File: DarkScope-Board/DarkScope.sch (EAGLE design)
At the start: 5 parts, among them IC1 ATSAME70Q21A-AN, X1 1-227161-0, X2 1-227161-0, X3 1-227161-0, X4 1-227161-0

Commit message: Added Circuits
Added circuitry for 4 channels and Op amps
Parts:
- removed X4: 1-227161-0, con-coax:1-227161-0
- added C1, C10, C18, C19, C27, C28, C36, C9: 0.1uf, rcl:C-EUC0603
- added C11, C2, C20, C29: 220pf, rcl:C-EUC0603
- added C12, C21, C3, C30: 3pf, rcl:C-EUC0603
- added C13, C22, C31, C4: 1PF, rcl:C-EUC0603
- added C14, C15, C23, C24, C32, C33, C5, C6: 30pf, rcl:C-TRIMM3018_11
- added C16, C17, C25, C26, C34, C35, C7, C8: 120pf, rcl:C-EUC0603
- added D1, D2, D3, D4: ss14, diode:SCHOTTKY-DIODESMD
- added IC2, IC3, IC4, IC5: TL084D, linear:TL084D
- added K1, K2, K3, K4: 4-1462037-0 (3V Version), SamacSys_Parts:4-1462037-0
- added R1, R19, R37, R55: 10M, rcl:R-US_R0603
- added R10, R14, R15, R28, R32, R33, R46, R50, R51, R64, R68, R69: 120, rcl:R-US_R0603
- added R11, R18, R29, R36, R47, R54, R65, R72: 1k, rcl:R-US_R0603
- added R12, R30, R48, R66: 3k, rcl:R-US_R0603
- added R13, R31, R49, R67: 1.5k, rcl:R-US_R0603
- added R16, R17, R21, R3, R34, R35, R39, R52, R53, R57, R70, R71: 100k, rcl:R-US_R0603
- added R2, R20, R38, R56: 1M, rcl:R-US_R0603
- added R22, R4, R40, R58: 1.8M, rcl:R-US_R0603
- added R23, R41, R5, R59: 2M, rcl:R-US_R0603
- added R24, R42, R6, R60: 200k, rcl:R-US_R0603
- added R25, R43, R61, R7: 20k, rcl:R-US_R0603
- added R26, R44, R62, R8: 300, rcl:R-US_R0603
- added R27, R45, R63, R9: 180, rcl:R-US_R0603
- added T1, T10, T11, T12, T13, T14, T15, T16, T17, T18, T19, T2, T20, T21, T22, T23, T24, T25, T26, T27, T28, T29, T3, T30, T31, T32, T33, T34, T35, T36, T37, T38, T39, T4, T40, T5, T6, T7, T8, T9: (no value), DC_LOAD_AU:BC817-40-NPN-SOT23-BEC
- added X5: 1-227161-0, con-coax:1-227161-0
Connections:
- new net +5V: R12.2, R30.2, R48.2, R66.2
- new net +5V/2: D1.C, D2.C, D3.C, D4.C, K1.8, K2.8, K3.8, K4.8
- new net GND: C14.A, C15.A, C16.2, C17.2, C18.2, C23.A, C24.A, C25.2, C26.2, C27.2, C32.A, C33.A, C34.2, C35.2, C36.2, C5.A, C6.A, C7.2, C8.2, C9.2, R10.2, R13.1, R2.1, R20.1, R24.2, R25.2, R28.2, R31.1, R38.1, R42.2, R43.2, R46.2, R49.1, R56.1, R6.2, R60.2, R61.2, R64.2, R67.1, R7.2, T1.E, T11.E, T14.C, T21.E, T24.C, T31.E, T34.C, T4.C, X1.2, X2.2, X3.2, X5.2
- new net N$1: D1.A, K1.1, T1.C
- new net N$10: C2.2, R3.1, T5.C
- new net N$100: R62.2, R63.1, T38.C
- new net N$101: R63.2, R64.1, T39.C
- new net N$102: T35.B
- new net N$103: T36.B
- new net N$104: T37.B
- new net N$105: T34.B
- new net N$106: T33.B
- new net N$107: T32.B
- new net N$108: IC5C.+IN, T38.E, T39.E, T40.E
- new net N$109: IC5C.-IN, R65.1, R66.1, R67.2
- new net N$11: C3.2, C5.E, R4.1, R6.1, T6.C
- new net N$110: IC5C.OUT, R65.2, R68.1, R69.2
- new net N$111: C35.1, R68.2
- new net N$112: IC5D.+IN, R69.1, R70.2
- new net N$113: IC5D.OUT, R70.1, R72.2
- new net N$114: C36.1, IC5D.-IN, R71.2
- new net N$115: R71.1
- new net N$116: R72.1
- new net N$12: R10.1, R9.2, T9.C
- new net N$13: IC2B.+IN, T5.E, T6.E, T7.E
- new net N$14: IC2B.-IN, IC2B.OUT, R8.1, T10.C
- new net N$15: T5.B
- new net N$16: T6.B
- new net N$17: T7.B
- new net N$18: T4.B
- new net N$19: T3.B
- new net N$2: T1.B
- new net N$20: T2.B
- new net N$21: IC2C.+IN, T10.E, T8.E, T9.E
- new net N$22: IC2C.-IN, R11.1, R12.1, R13.2
- new net N$23: IC2C.OUT, R11.2, R14.1, R15.2
- new net N$24: C8.1, R14.2
- new net N$25: IC2D.+IN, R15.1, R16.2
- new net N$26: IC2D.OUT, R16.1, R18.2
- new net N$27: C9.1, IC2D.-IN, R17.2
- new net N$28: R17.1
- new net N$29: R18.1
- new net N$3: C1.2, T3.C
- new net N$30: D2.A, K2.1, T11.C
- new net N$31: K2.6, X5.1
- new net N$32: C10.1, K2.7, R19.1, R20.2, T12.C
- new net N$33: K2.5, R19.2
- new net N$34: T11.B
- new net N$35: C10.2, T13.C
- new net N$36: C11.1, C12.1, C13.1, R21.2, R22.2, R23.2, T12.E, T13.E, T14.E
- new net N$37: C11.2, R21.1, T15.C
- new net N$38: C12.2, C14.E, R22.1, R24.1, T16.C
- new net N$39: C13.2, C15.E, C16.1, R23.1, R25.1, T17.C
- new net N$4: K1.6, X1.1
- new net N$40: IC3B.+IN, T15.E, T16.E, T17.E
- new net N$41: IC3B.-IN, IC3B.OUT, R26.1, T20.C
- new net N$42: R26.2, R27.1, T18.C
- new net N$43: R27.2, R28.1, T19.C
- new net N$44: T15.B
- new net N$45: T16.B
- new net N$46: T17.B
- new net N$47: T14.B
- new net N$48: T13.B
- new net N$49: T12.B
- new net N$5: R8.2, R9.1, T8.C
- new net N$50: IC3C.+IN, T18.E, T19.E, T20.E
- new net N$51: IC3C.-IN, R29.1, R30.1, R31.2
- new net N$52: IC3C.OUT, R29.2, R32.1, R33.2
- new net N$53: C17.1, R32.2
- new net N$54: IC3D.+IN, R33.1, R34.2
- new net N$55: IC3D.OUT, R34.1, R36.2
- new net N$56: C18.1, IC3D.-IN, R35.2
- new net N$57: R35.1
- new net N$58: R36.1
- new net N$59: D3.A, K3.1, T21.C
- new net N$6: C1.1, K1.7, R1.1, R2.2, T2.C
- new net N$60: K3.6, X2.1
- new net N$61: C19.1, K3.7, R37.1, R38.2, T22.C
- new net N$62: K3.5, R37.2
- new net N$63: T21.B
- new net N$64: C19.2, T23.C
- new net N$65: C20.1, C21.1, C22.1, R39.2, R40.2, R41.2, T22.E, T23.E, T24.E
- new net N$66: C20.2, R39.1, T25.C
- new net N$67: C21.2, C23.E, R40.1, R42.1, T26.C
- new net N$68: C22.2, C24.E, C25.1, R41.1, R43.1, T27.C
- new net N$69: IC4B.+IN, T25.E, T26.E, T27.E
- new net N$7: K1.5, R1.2
- new net N$70: IC4B.-IN, IC4B.OUT, R44.1, T30.C
- new net N$71: R44.2, R45.1, T28.C
- new net N$72: R45.2, R46.1, T29.C
- new net N$73: T25.B
- new net N$74: T26.B
- new net N$75: T27.B
- new net N$76: T24.B
- new net N$77: T23.B
- new net N$78: T22.B
- new net N$79: IC4C.+IN, T28.E, T29.E, T30.E
- new net N$8: C2.1, C3.1, C4.1, R3.2, R4.2, R5.2, T2.E, T3.E, T4.E
- new net N$80: IC4C.-IN, R47.1, R48.1, R49.2
- new net N$81: IC4C.OUT, R47.2, R50.1, R51.2
- new net N$82: C26.1, R50.2
- new net N$83: IC4D.+IN, R51.1, R52.2
- new net N$84: IC4D.OUT, R52.1, R54.2
- new net N$85: C27.1, IC4D.-IN, R53.2
- new net N$86: R53.1
- new net N$87: R54.1
- new net N$88: D4.A, K4.1, T31.C
- new net N$89: K4.6, X3.1
- new net N$9: C4.2, C6.E, C7.1, R5.1, R7.1, T7.C
- new net N$90: C28.1, K4.7, R55.1, R56.2, T32.C
- new net N$91: K4.5, R55.2
- new net N$92: T31.B
- new net N$93: C28.2, T33.C
- new net N$94: C29.1, C30.1, C31.1, R57.2, R58.2, R59.2, T32.E, T33.E, T34.E
- new net N$95: C29.2, R57.1, T35.C
- new net N$96: C30.2, C32.E, R58.1, R60.1, T36.C
- new net N$97: C31.2, C33.E, C34.1, R59.1, R61.1, T37.C
- new net N$98: IC5B.+IN, T35.E, T36.E, T37.E
- new net N$99: IC5B.-IN, IC5B.OUT, R62.1, T40.C
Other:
- note added: "4.5"/7" LCD"
- note added: "HIGH SPEED ADC"
- note added: "HV Range Resistors"
- note added: "RCA Out"
- note added: "Sample Wave"
- note added: "Switches"
- note added: "Switching Circuitry"
- note added: "USB and Charging Circuitry"
- note added: "VGA Out"

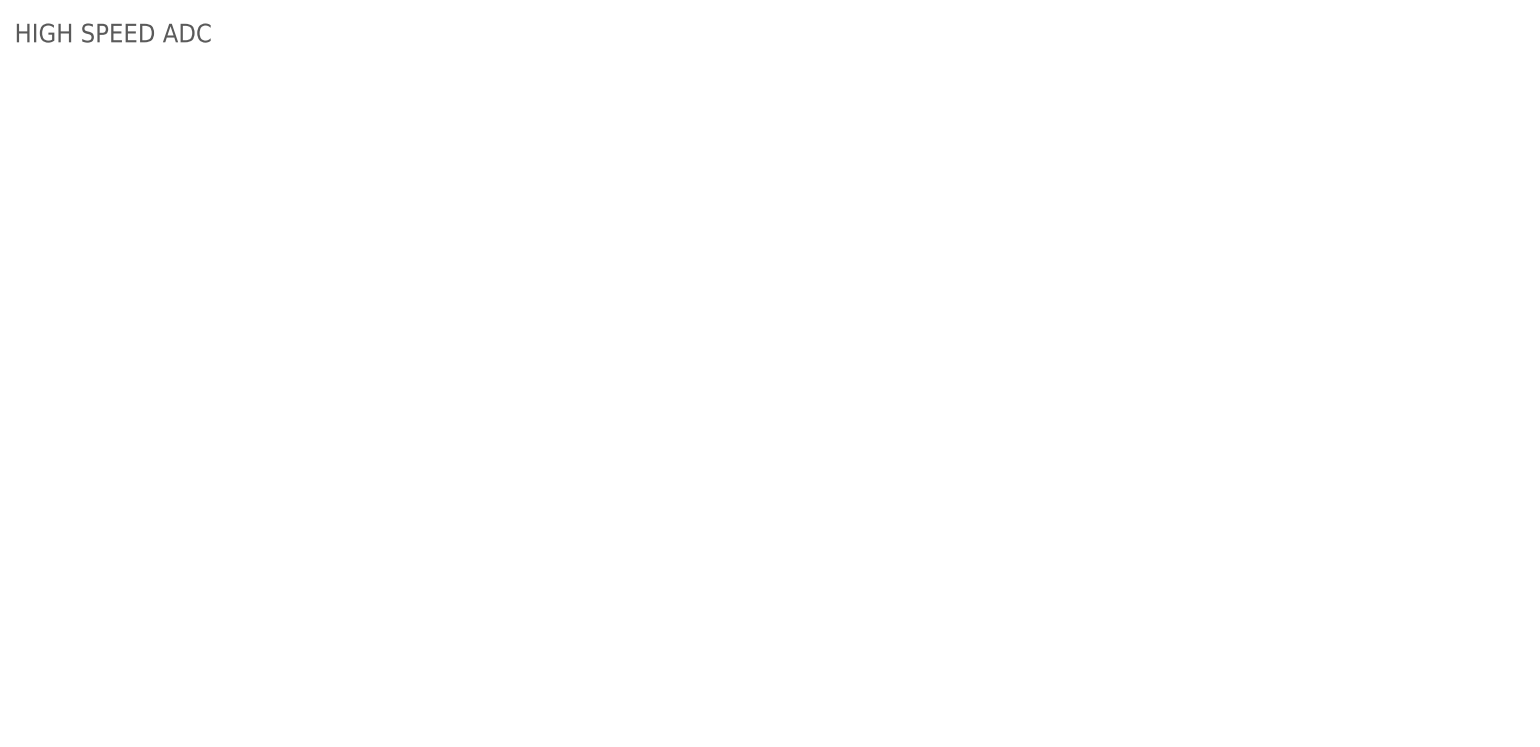
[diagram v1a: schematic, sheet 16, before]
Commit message: Selected and Added More Devices
Added ADC,Battery Management IC,Flash and more.
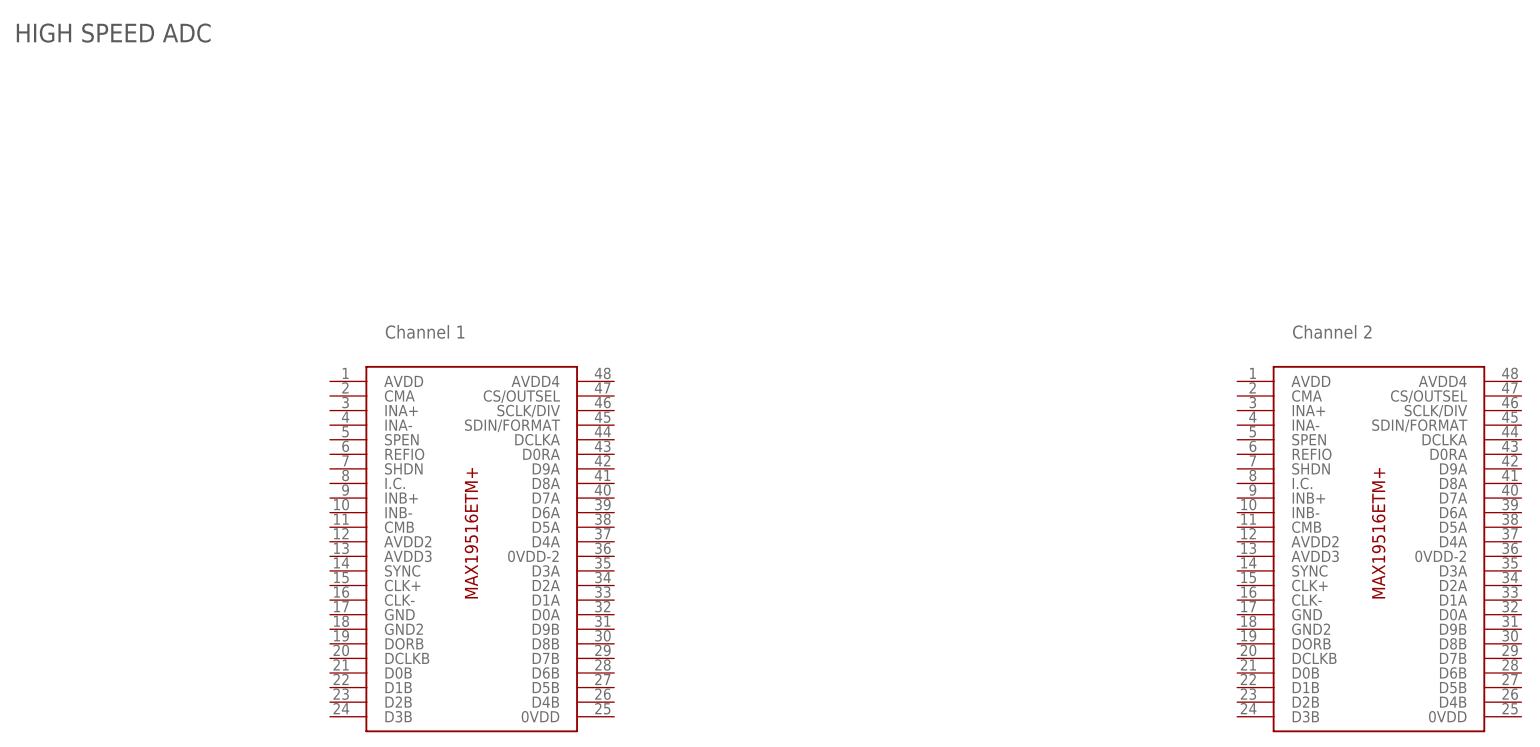
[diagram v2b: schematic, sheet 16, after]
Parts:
- added IC6, IC7: AT45DB161E-SSHD-T, SamacSys_Parts:AT45DB161E-SSHD-T
- added IC8: MCP73871-2CAI_ML, SamacSys_Parts:MCP73871-2CAI_ML
- added U$20, U$21: MAX19516ETM+MAX19516ETM+, Boltz_RnD:MAX19516ETM+MAX19516ETM+
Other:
- note added: "Channel 1"
- note added: "Channel 2"
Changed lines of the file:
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@@
 <grid distance="0.1" unitdist="inch" unit="inch" style="lines" multiple="1" display="no" altdistance="0.01" altunitdist="inch" altunit="inch"/>
 <layers>
-<layer number="1" name="Top" color="4" fill="1" visible="yes" active="no"/>
-<layer number="2" name="Route2" color="1" fill="3" visible="yes" active="no"/>
-<layer number="3" name="Route3" color="4" fill="3" visible="yes" active="no"/>
-<layer number="4" name="Route4" color="1" fill="4" visible="yes" active="no"/>
-<layer number="5" name="Route5" color="4" fill="4" visible="yes" active="no"/>
-<layer number="6" name="Route6" color="1" fill="8" visible="yes" active="no"/>
-<layer number="7" name="Route7" color="4" fill="8" visible="yes" active="no"/>
-<layer number="8" name="Route8" color="1" fill="2" visible="yes" active="no"/>
-<layer number="9" name="Route9" color="4" fill="2" visible="yes" active="no"/>
-<layer number="10" name="Route10" color="1" fill="7" visible="yes" active="no"/>
-<layer number="11" name="Route11" color="4" fill="7" visible="yes" active="no"/>
-<layer number="12" name="Route12" color="1" fill="5" visible="yes" active="no"/>
-<layer number="13" name="Route13" color="4" fill="5" visible="yes" active="no"/>
-<layer number="14" name="Route14" color="1" fill="6" visible="yes" active="no"/>
-<layer number="15" name="Route15" color="4" fill="6" visible="yes" active="no"/>
-<layer number="16" name="Bottom" color="1" fill="1" visible="yes" active="no"/>
-<layer number="17" name="Pads" color="2" fill="1" visible="yes" active="no"/>
-<layer number="18" name="Vias" color="2" fill="1" visible="yes" active="no"/>
-<layer number="19" name="Unrouted" color="6" fill="1" visible="yes" active="no"/>
-<layer number="20" name="Dimension" color="24" fill="1" visible="yes" active="no"/>
-<layer number="21" name="tPlace" color="7" fill="1" visible="yes" active="no"/>
-<layer number="22" name="bPlace" color="7" fill="1" visible="yes" active="no"/>
-<layer number="23" name="tOrigins" color="15" fill="1" visible="yes" active="no"/>
-<layer number="24" name="bOrigins" color="15" fill="1" visible="yes" active="no"/>
-<layer number="25" name="tNames" color="7" fill="1" visible="yes" active="no"/>
-<layer number="26" name="bNames" color="7" fill="1" visible="yes" active="no"/>
-<layer number="27" name="tValues" color="7" fill="1" visible="yes" active="no"/>
-<layer number="28" name="bValues" color="7" fill="1" visible="yes" active="no"/>
+<layer number="1" name="Top" color="4" fill="1" visible="no" active="no"/>
+<layer number="2" name="Route2" color="1" fill="3" visible="no" active="no"/>
+<layer number="3" name="Route3" color="4" fill="3" visible="no" active="no"/>
+<layer number="4" name="Route4" color="1" fill="4" visible="no" active="no"/>
+<layer number="5" name="Route5" color="4" fill="4" visible="no" active="no"/>
+<layer number="6" name="Route6" color="1" fill="8" visible="no" active="no"/>
+<layer number="7" name="Route7" color="4" fill="8" visible="no" active="no"/>
+<layer number="8" name="Route8" color="1" fill="2" visible="no" active="no"/>
+<layer number="9" name="Route9" color="4" fill="2" visible="no" active="no"/>
+<layer number="10" name="Route10" color="1" fill="7" visible="no" active="no"/>
+<layer number="11" name="Route11" color="4" fill="7" visible="no" active="no"/>
+<layer number="12" name="Route12" color="1" fill="5" visible="no" active="no"/>
+<layer number="13" name="Route13" color="4" fill="5" visible="no" active="no"/>
+<layer number="14" name="Route14" color="1" fill="6" visible="no" active="no"/>
+<layer number="15" name="Route15" color="4" fill="6" visible="no" active="no"/>
+<layer number="16" name="Bottom" color="1" fill="1" visible="no" active="no"/>
+<layer number="17" name="Pads" color="2" fill="1" visible="no" active="no"/>
+<layer number="18" name="Vias" color="2" fill="1" visible="no" active="no"/>
+<layer number="19" name="Unrouted" color="6" fill="1" visible="no" active="no"/>
+<layer number="20" name="Dimension" color="24" fill="1" visible="no" active="no"/>
+<layer number="21" name="tPlace" color="7" fill="1" visible="no" active="no"/>
+<layer number="22" name="bPlace" color="7" fill="1" visible="no" active="no"/>
+<layer number="23" name="tOrigins" color="15" fill="1" visible="no" active="no"/>
+<layer number="24" name="bOrigins" color="15" fill="1" visible="no" active="no"/>
+<layer number="25" name="tNames" color="7" fill="1" visible="no" active="no"/>
+<layer number="26" name="bNames" color="7" fill="1" visible="no" active="no"/>
+<layer number="27" name="tValues" color="7" fill="1" visible="no" active="no"/>
+<layer number="28" name="bValues" color="7" fill="1" visible="no" active="no"/>
 <layer number="29" name="tStop" color="7" fill="3" visible="no" active="no"/>
 <layer number="30" name="bStop" color="7" fill="6" visible="no" active="no"/>
@@
 <layer number="35" name="tGlue" color="7" fill="4" visible="no" active="no"/>
 <layer number="36" name="bGlue" color="7" fill="5" visible="no" active="no"/>
-<layer number="37" name="tTest" color="7" fill="1" visible="yes" active="no"/>
-<layer number="38" name="bTest" color="7" fill="1" visible="yes" active="no"/>
+<layer number="37" name="tTest" color="7" fill="1" visible="no" active="no"/>
+<layer number="38" name="bTest" color="7" fill="1" visible="no" active="no"/>
 <layer number="39" name="tKeepout" color="4" fill="11" visible="no" active="no"/>
 <layer number="40" name="bKeepout" color="1" fill="11" visible="no" active="no"/>
@@
 <layer number="44" name="Drills" color="7" fill="1" visible="no" active="no"/>
 <layer number="45" name="Holes" color="7" fill="1" visible="no" active="no"/>
-<layer number="46" name="Milling" color="3" fill="1" visible="yes" active="no"/>
-<layer number="47" name="Measures" color="7" fill="1" visible="yes" active="no"/>
-<layer number="48" name="Document" color="7" fill="1" visible="yes" active="no"/>
-<layer number="49" name="Reference" color="7" fill="1" visible="yes" active="no"/>
-<layer number="50" name="dxf" color="7" fill="1" visible="yes" active="no"/>
-<layer number="51" name="tDocu" color="7" fill="1" visible="yes" active="no"/>
-<layer number="52" name="bDocu" color="7" fill="1" visible="yes" active="no"/>
-<layer number="53" name="tGND_GNDA" color="7" fill="1" visible="yes" active="no"/>
-<layer number="54" name="bGND_GNDA" color="7" fill="1" visible="yes" active="no"/>
-<layer number="56" name="wert" color="7" fill="1" visible="yes" active="no"/>
-<layer number="57" name="tCAD" color="7" fill="1" visible="yes" active="no"/>
+<layer number="46" name="Milling" color="3" fill="1" visible="no" active="no"/>
+<layer number="47" name="Measures" color="7" fill="1" visible="no" active="no"/>
+<layer number="48" name="Document" color="7" fill="1" visible="no" active="no"/>
+<layer number="49" name="Reference" color="7" fill="1" visible="no" active="no"/>
+<layer number="50" name="dxf" color="7" fill="1" visible="no" active="no"/>
+<layer number="51" name="tDocu" color="7" fill="1" visible="no" active="no"/>
+<layer number="52" name="bDocu" color="7" fill="1" visible="no" active="no"/>
+<layer number="53" name="tGND_GNDA" color="7" fill="1" visible="no" active="no"/>
+<layer number="54" name="bGND_GNDA" color="7" fill="1" visible="no" active="no"/>
+<layer number="56" name="wert" color="7" fill="1" visible="no" active="no"/>
+<layer number="57" name="tCAD" color="7" fill="1" visible="no" active="no"/>
 <layer number="88" name="SimResults" color="9" fill="1" visible="yes" active="yes"/>
 <layer number="89" name="SimProbes" color="9" fill="1" visible="yes" active="yes"/>
@@
 <part name="R72" library="rcl" library_urn="urn:adsk.eagle:library:334" deviceset="R-US_" device="R0603" package3d_urn="urn:adsk.eagle:package:23555/2" value="1k"/>
 <part name="SUPPLY40" library="supply2" library_urn="urn:adsk.eagle:library:372" deviceset="GND" device=""/>
+<part name="U$20" library="Boltz_RnD" deviceset="MAX19516ETM+" device="MAX19516ETM+" package3d_urn="urn:adsk.eagle:package:3608124/1"/>
+<part name="U$21" library="Boltz_RnD" deviceset="MAX19516ETM+" device="MAX19516ETM+" package3d_urn="urn:adsk.eagle:package:3608124/1"/>
+<part name="IC6" library="SamacSys_Parts" deviceset="AT45DB161E-SSHD-T" device=""/>
+<part name="IC7" library="SamacSys_Parts" deviceset="AT45DB161E-SSHD-T" device=""/>
+<part name="IC8" library="SamacSys_Parts" deviceset="MCP73871-2CAI_ML" device=""/>
 </parts>
 <sheets>
@@
 <pinref part="T8" gate="G$1" pin="C"/>
 <junction x="223.52" y="165.1"/>
-<pinref part="T8" gate="G$1" pin="C"/>
 <wire x1="223.52" y1="165.1" x2="213.36" y2="165.1" width="0.1524" layer="91"/>
 <junction x="213.36" y="165.1"/>
@@
 <pinref part="T9" gate="G$1" pin="C"/>
 <junction x="223.52" y="154.94"/>
-<pinref part="T9" gate="G$1" pin="C"/>
 <wire x1="223.52" y1="154.94" x2="213.36" y2="154.94" width="0.1524" layer="91"/>
 <junction x="213.36" y="154.94"/>
@@
 <instances>
 <instance part="U$7" gate="G$1" x="0" y="0"/>
+<instance part="IC6" gate="G$1" x="60.96" y="152.4"/>
+<instance part="IC7" gate="G$1" x="195.58" y="152.4"/>
 </instances>
 <busses>
@@
 <instances>
 <instance part="U$8" gate="G$1" x="0" y="0"/>
+<instance part="IC8" gate="G$1" x="86.36" y="129.54"/>
 </instances>
 <busses>
@@
 <plain>
 <text x="17.78" y="198.12" size="2.54" layer="97">HIGH SPEED ADC</text>
+<text x="68.58" y="157.48" size="1.778" layer="95">Channel 1</text>
+<text x="193.04" y="157.48" size="1.778" layer="95">Channel 2</text>
 </plain>
 <instances>
 <instance part="U$16" gate="G$1" x="0" y="0"/>
+<instance part="U$20" gate="G$1" x="66.04" y="101.6"/>
+<instance part="U$21" gate="G$1" x="190.5" y="101.6"/>
 </instances>
 <busses>
